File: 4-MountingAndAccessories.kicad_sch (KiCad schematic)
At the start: 11 parts, among them J001 Spring Contact, P401 Molex PicoBlade

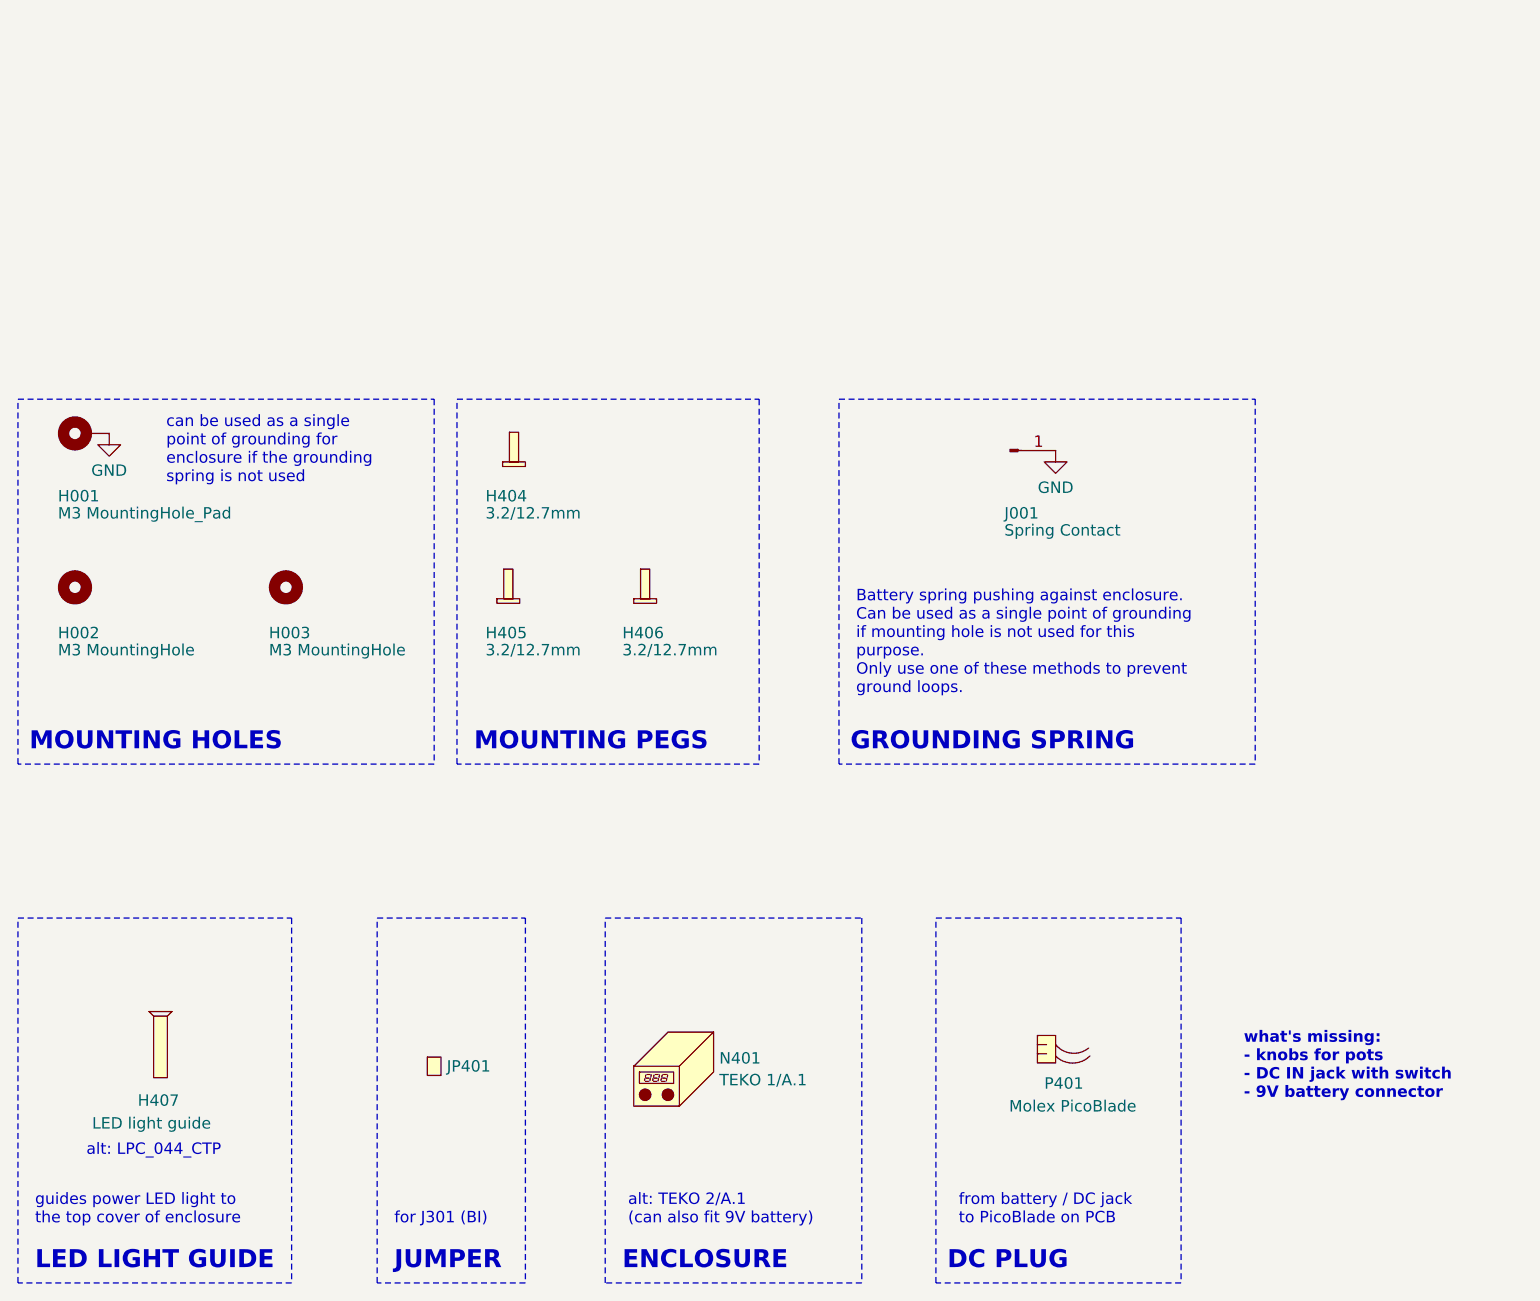
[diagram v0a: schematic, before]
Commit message: improving the schematic - v3.0. Very crude draft of board layout with battery holder underneath the PCB
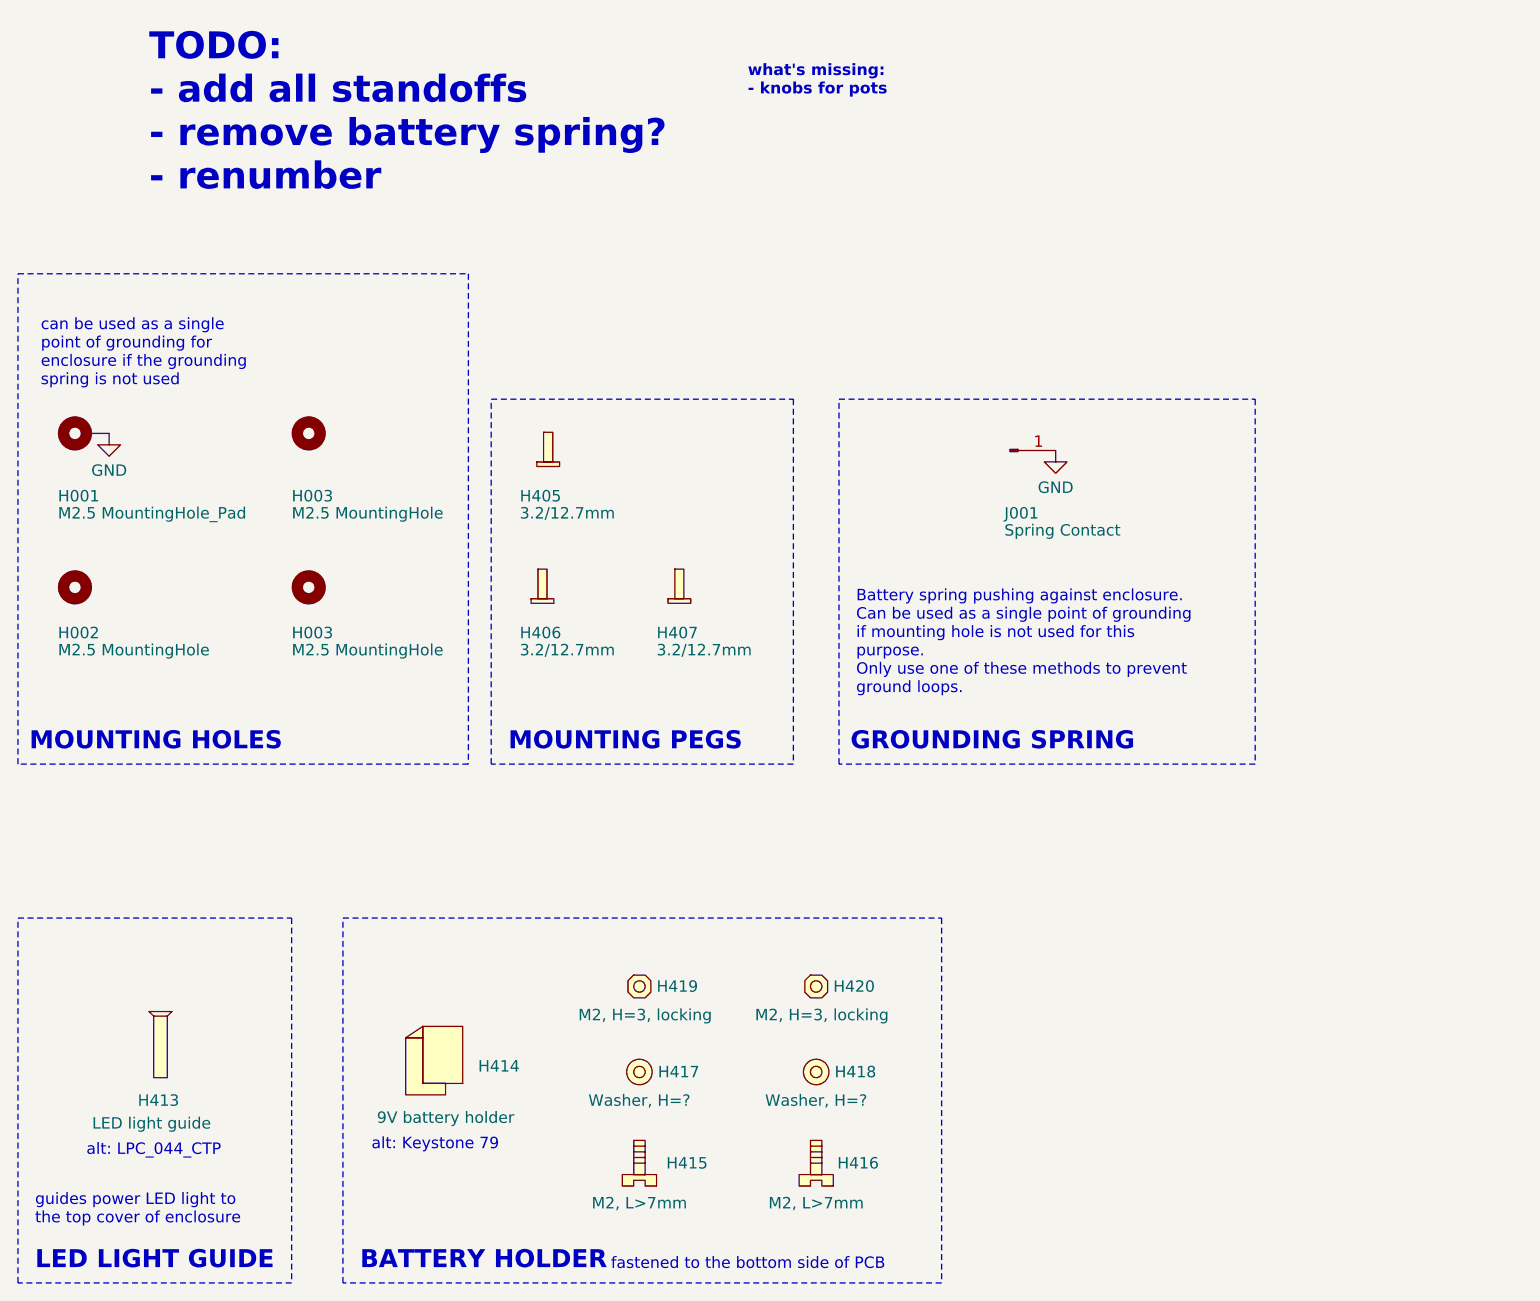
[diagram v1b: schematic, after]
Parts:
- removed JP401: ~, symbol jumper:Jumper
- removed N401: TEKO 1/A.1, symbol Mechanical:Housing
- removed P401: Molex PicoBlade, symbol MolexPicoBladePlug:MolexPicoBladePlug
- added H003: M2.5 MountingHole, MountingHole:MountingHole_2.7mm_M2.5_ISO14580, symbol Mechanical:MountingHole
- added H414: 9V battery holder, library:KEYSTONE-71, symbol 9VBatteryHolder:9VBatteryHolder
- added H415, H416: M2, L>7mm, symbol Bolt:Bolt
- added H417, H418: Washer, H=?, symbol Washer:Washer
- added H419, H420: M2, H=3, locking, symbol Nut:Nut
- H001: value M3 MountingHole_Pad -> M2.5 MountingHole_Pad; footprint MountingHole:MountingHole_3.2mm_M3_ISO14580_Pad -> MountingHole:MountingHole_2.7mm_M2.5_ISO14580_Pad
- H002, H003: value M3 MountingHole -> M2.5 MountingHole; footprint MountingHole:MountingHole_3.2mm_M3_ISO14580 -> MountingHole:MountingHole_2.7mm_M2.5_ISO14580
- renumbered H404 to H405, H405 to H406, H406 to H407, H407 to H413
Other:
- note added: "BATTERY HOLDER"
- note added: "TODO: - add all standoffs - remove battery spring? - renumber"
- note added: "alt: Keystone 79"
- note added: "fastened to the bottom side of PCB"
- note added: "what's missing: - knobs for pots"
- note removed: "DC PLUG"
- note removed: "ENCLOSURE"
- note removed: "JUMPER"
- note removed: "alt: TEKO 2/A.1 (can also fit 9V battery)"
- note removed: "for J301 (BI)"
- note removed: "from battery / DC jack to PicoBlade on PCB"
- note removed: "what's missing: - knobs for pots - DC IN jack with switch - 9V battery connector"
- moved on the sheet: H003, H405, H406, H407

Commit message: saving in Kicad8 for the first time - some underlying formats changed
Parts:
- renumbered H001 to H401, H003 to H402, H002 to H403, H003 to H404, J001 to J401
